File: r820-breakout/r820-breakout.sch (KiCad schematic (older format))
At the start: 18 parts, among them J1 Conn_Coaxial, J2 Conn_01x10, J3 Conn_01x02, J4 Conn_01x02, U1 R820T, Y1 16MHz CL=16pF

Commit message: Heavily reworked.
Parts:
- removed J3: Conn_01x02, Connector_PinHeader_2.54mm:PinHeader_1x02_P2.54mm_Vertical, symbol Connector_Generic:Conn_01x02
- removed Y1: 16MHz CL=16pF, Crystal:Crystal_HC49-4H_Vertical, symbol Device:Crystal_Small
- added C10, C11: C, Capacitors_SMD:C_0402, symbol device:C
- added C12: 330p, Capacitors_SMD:C_0603, symbol device:C
- added C13: 10n, Capacitors_SMD:C_0603, symbol device:C
- added C14: 100n, Capacitors_SMD:C_0603, symbol device:C
- added C15, C16: 100nF, Capacitors_SMD:C_0402, symbol r820-breakout-rescue:C_Small-Device
- added D1: BAV99, TO_SOT_Packages_SMD:SOT-23, symbol Diode:BAV99
- added L3: 8.2n, Inductors_SMD:L_0603, symbol device:L
- added L4: 180n, Inductors_SMD:L_0603, symbol device:L
- added Y1: Crystal_GND24, Crystals:Crystal_SMD_TXC_7M-4pin_3.2x2.5mm, symbol device:Crystal_GND24
- C1, C2, C3, C5: footprint Capacitor_SMD:C_0603_1608Metric -> Capacitors_SMD:C_0402; symbol Device:C_Small -> r820-breakout-rescue:C_Small-Device
- C4, C6, C7, C8, C9: symbol Device:C_Small -> r820-breakout-rescue:C_Small-Device
- J1: footprint Connector_Coaxial:SMA_Molex_73251-2200_Horizontal -> Connectors_Molex:Molex_SMA_Jack_Edge_Mount; symbol Connector:Conn_Coaxial -> r820-breakout-rescue:Conn_Coaxial-Connector
- J2: symbol Connector_Generic:Conn_01x10 -> r820-breakout-rescue:Conn_01x10-Connector_Generic
- J4: symbol Connector_Generic:Conn_01x02 -> r820-breakout-rescue:Conn_01x02-Connector_Generic
- L1, L2: symbol Device:L -> r820-breakout-rescue:L-Device
- R1: symbol Device:R -> r820-breakout-rescue:R-Device
- U1: footprint Sensor_Motion:InvenSense_QFN-24_4x4mm_P0.5mm -> Housings_DFN_QFN:QFN-24-1EP_4x4mm_Pitch0.5mm; symbol RafaelMicro:R820T -> r820-breakout-rescue:R820T-RafaelMicro
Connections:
- net GND: now also J2.2 (Pin_2), J2.5 (Pin_5), J2.7 (Pin_7), U1.25 (EXPAD), C14.1, C15.1, C16.1, D1.1 (A), D1.2 (K), Y1.2, Y1.4; no longer J2.3 (Pin_3), J2.4 (Pin_4), J4.1 (Pin_1)
- net T_CLK_Out: now also J2.6 (Pin_6); no longer J2.7 (Pin_7)
- net T_IF_N: now also C10.2; no longer U1.12 (IF_N)
- net T_IF_P: now also C11.2; no longer U1.13 (IF_P)
- net T_RF_IN: now also C13.1, L4.2; no longer U1.24 (RF-IN)
- net T_SCL: now also J2.3 (Pin_3); no longer J2.6 (Pin_6)
- net T_SDA: now also J2.4 (Pin_4); no longer J2.5 (Pin_5)
- net VDD_3V: now also C15.2, C16.2; no longer J2.2 (Pin_2)
- net at C7.1, U1.8 (XTAL_I): now also Y1.3
- net at C6.1, U1.9 (XTAL_O): now also Y1.1
- new net: C10.1, U1.12 (IF_N)
- new net: C11.1, U1.13 (IF_P)
- new net: L3.2, U1.24 (RF-IN)
- new net: C12.2, L3.1
- new net: C14.2, J4.1 (Pin_1), L4.1
- new net: C12.1, C13.2, D1.3 (A), D1.3 (K)
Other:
- moved on the sheet: J4

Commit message: footprint fix, added OSH logo, removed big via under rt820t
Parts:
- C1, C15, C16, C2, C3, C5: footprint Capacitors_SMD:C_0402 -> Capacitor_SMD:C_0402_1005Metric; symbol r820-breakout-rescue:C_Small-Device -> r820-breakout-rescue:C_Small-Device-r820-breakout-rescue
- C10, C11: footprint Capacitors_SMD:C_0402 -> Capacitor_SMD:C_0402_1005Metric; symbol device:C -> r820-breakout-rescue:C-device
- C12, C13, C14: footprint Capacitors_SMD:C_0603 -> Capacitor_SMD:C_0603_1608Metric; symbol device:C -> r820-breakout-rescue:C-device
- C4, C6, C7, C8, C9: symbol r820-breakout-rescue:C_Small-Device -> r820-breakout-rescue:C_Small-Device-r820-breakout-rescue
- D1: footprint TO_SOT_Packages_SMD:SOT-23 -> Package_TO_SOT_SMD:SOT-23
- J1: symbol r820-breakout-rescue:Conn_Coaxial-Connector -> r820-breakout-rescue:Conn_Coaxial-Connector-r820-breakout-rescue
- J2: symbol r820-breakout-rescue:Conn_01x10-Connector_Generic -> r820-breakout-rescue:Conn_01x10-Connector_Generic-r820-breakout-rescue
- J4: symbol r820-breakout-rescue:Conn_01x02-Connector_Generic -> r820-breakout-rescue:Conn_01x02-Connector_Generic-r820-breakout-rescue
- L1, L2: symbol r820-breakout-rescue:L-Device -> r820-breakout-rescue:L-Device-r820-breakout-rescue
- L3, L4: footprint Inductors_SMD:L_0603 -> Inductor_SMD:L_0603_1608Metric; symbol device:L -> r820-breakout-rescue:L-device
- R1: symbol r820-breakout-rescue:R-Device -> r820-breakout-rescue:R-Device-r820-breakout-rescue
- U1: footprint Housings_DFN_QFN:QFN-24-1EP_4x4mm_Pitch0.5mm -> Package_DFN_QFN:QFN-24-1EP_4x4mm_P0.5mm_EP2.7x2.7mm_ThermalVias; symbol r820-breakout-rescue:R820T-RafaelMicro -> r820-breakout-rescue:R820T-RafaelMicro-r820-breakout-rescue
- Y1: footprint Crystals:Crystal_SMD_TXC_7M-4pin_3.2x2.5mm -> Crystal:Crystal_SMD_TXC_7M-4Pin_3.2x2.5mm; symbol device:Crystal_GND24 -> r820-breakout-rescue:Crystal_GND24-device
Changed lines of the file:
@@
 $EndDescr
 $Comp
-L r820-breakout-rescue:R820T-RafaelMicro U1
+L r820-breakout-rescue:R820T-RafaelMicro-r820-breakout-rescue U1
 U 1 1 5CDEF36B
 P 4400 3650
 F 0 "U1" H 4800 2850 50  0000 C CNN
 F 1 "R820T" H 4800 2750 50  0000 C CNN
-F 2 "Housings_DFN_QFN:QFN-24-1EP_4x4mm_Pitch0.5mm" H 4450 3650 50  0001 C CNN
+F 2 "Package_DFN_QFN:QFN-24-1EP_4x4mm_P0.5mm_EP2.7x2.7mm_ThermalVias" H 4450 3650 50  0001 C CNN
 F 3 "" H 4450 3650 50  0001 C CNN
 	1    4400 3650
@@
 $EndComp
 $Comp
-L r820-breakout-rescue:C_Small-Device C5
+L r820-breakout-rescue:C_Small-Device-r820-breakout-rescue C5
 U 1 1 5CDEF46F
 P 3100 3200
 F 0 "C5" V 3329 3200 50  0000 C CNN
 F 1 "100nF" V 3238 3200 50  0000 C CNN
-F 2 "Capacitors_SMD:C_0402" H 3100 3200 50  0001 C CNN
+F 2 "Capacitor_SMD:C_0402_1005Metric" H 3100 3200 50  0001 C CNN
 F 3 "~" H 3100 3200 50  0001 C CNN
 	1    3100 3200
@@
 $EndComp
 $Comp
-L r820-breakout-rescue:C_Small-Device C4
+L r820-breakout-rescue:C_Small-Device-r820-breakout-rescue C4
 U 1 1 5CDEF4C6
 P 2700 3100
@@
 $EndComp
 $Comp
-L r820-breakout-rescue:C_Small-Device C6
+L r820-breakout-rescue:C_Small-Device-r820-breakout-rescue C6
 U 1 1 5CDEF8DA
 P 2850 4300
@@
 $EndComp
 $Comp
-L r820-breakout-rescue:C_Small-Device C7
+L r820-breakout-rescue:C_Small-Device-r820-breakout-rescue C7
 U 1 1 5CDEF920
 P 3150 4300
@@
 T_IF_AGC
 $Comp
-L r820-breakout-rescue:R-Device R1
+L r820-breakout-rescue:R-Device-r820-breakout-rescue R1
 U 1 1 5CDF60D3
 P 5850 4150
@@
 $EndComp
 $Comp
-L r820-breakout-rescue:C_Small-Device C9
+L r820-breakout-rescue:C_Small-Device-r820-breakout-rescue C9
 U 1 1 5CDF73BF
 P 6250 4500
@@
 $EndComp
 $Comp
-L r820-breakout-rescue:C_Small-Device C8
+L r820-breakout-rescue:C_Small-Device-r820-breakout-rescue C8
 U 1 1 5CDF86FE
 P 5850 4500
@@
 	5500 3950 5000 3950
 $Comp
-L r820-breakout-rescue:L-Device L2
+L r820-breakout-rescue:L-Device-r820-breakout-rescue L2
 U 1 1 5CE049F6
 P 5300 3650
@@
 $EndComp
 $Comp
-L r820-breakout-rescue:L-Device L1
+L r820-breakout-rescue:L-Device-r820-breakout-rescue L1
 U 1 1 5CE06D89
 P 5300 3450
@@
 $EndComp
 $Comp
-L r820-breakout-rescue:C_Small-Device C3
+L r820-breakout-rescue:C_Small-Device-r820-breakout-rescue C3
 U 1 1 5CE0C2BA
 P 4700 2450
-F 0 "C3" H 5400 2500 50  0000 L CNN
-F 1 "100nF" H 5400 2400 50  0000 L CNN
-F 2 "Capacitors_SMD:C_0402" H 4700 2450 50  0001 C CNN
+F 0 "C3" H 4700 3200 50  0000 L CNN
+F 1 "100nF" H 4700 3100 50  0000 L CNN
+F 2 "Capacitor_SMD:C_0402_1005Metric" H 4700 2450 50  0001 C CNN
 F 3 "~" H 4700 2450 50  0001 C CNN
 	1    4700 2450
@@
 $EndComp
 $Comp
-L r820-breakout-rescue:C_Small-Device C2
+L r820-breakout-rescue:C_Small-Device-r820-breakout-rescue C2
 U 1 1 5CE0C345
 P 4500 2450
-F 0 "C2" H 5150 2500 50  0000 L CNN
-F 1 "10nF" H 5150 2400 50  0000 L CNN
-F 2 "Capacitors_SMD:C_0402" H 4500 2450 50  0001 C CNN
+F 0 "C2" H 4500 3200 50  0000 L CNN
+F 1 "10nF" H 4500 3100 50  0000 L CNN
+F 2 "Capacitor_SMD:C_0402_1005Metric" H 4500 2450 50  0001 C CNN
 F 3 "~" H 4500 2450 50  0001 C CNN
 	1    4500 2450
@@
 NoConn ~ 5000 3050
 $Comp
-L r820-breakout-rescue:C_Small-Device C1
+L r820-breakout-rescue:C_Small-Device-r820-breakout-rescue C1
 U 1 1 5CE150EA
 P 4300 2450
-F 0 "C1" H 4850 2500 50  0000 L CNN
-F 1 "100nF" H 4850 2400 50  0000 L CNN
-F 2 "Capacitors_SMD:C_0402" H 4300 2450 50  0001 C CNN
+F 0 "C1" H 4300 3400 50  0000 L CNN
+F 1 "100nF" H 4300 3300 50  0000 L CNN
+F 2 "Capacitor_SMD:C_0402_1005Metric" H 4300 2450 50  0001 C CNN
 F 3 "~" H 4300 2450 50  0001 C CNN
 	1    4300 2450
@@
 	9100 2900 8900 2900
 $Comp
-L r820-breakout-rescue:Conn_Coaxial-Connector J1
+L r820-breakout-rescue:Conn_Coaxial-Connector-r820-breakout-rescue J1
 U 1 1 5CE52A4C
 P 9300 1300
@@
 	9300 1500 9300 1600
 $Comp
-L r820-breakout-rescue:Conn_01x02-Connector_Generic J4
+L r820-breakout-rescue:Conn_01x02-Connector_Generic-r820-breakout-rescue J4
 U 1 1 5CE56D37
 P 7520 2790
@@
 	3600 3950 3600 4900
 $Comp
-L device:Crystal_GND24 Y1
+L r820-breakout-rescue:Crystal_GND24-device Y1
 U 1 1 5CE32966
 P 3000 3960
 F 0 "Y1" H 2810 4006 50  0000 R CNN
 F 1 "Crystal_GND24" H 2810 3915 50  0000 R CNN
-F 2 "Crystals:Crystal_SMD_TXC_7M-4pin_3.2x2.5mm" H 3000 3960 50  0001 C CNN
+F 2 "Crystal:Crystal_SMD_TXC_7M-4Pin_3.2x2.5mm" H 3000 3960 50  0001 C CNN
 F 3 "" H 3000 3960 50  0001 C CNN
 	1    3000 3960
@@
 	8900 2400 9100 2400
 $Comp
-L device:C C10
+L r820-breakout-rescue:C-device C10
 U 1 1 5CE3EC04
 P 5300 4300
 F 0 "C10" H 5415 4346 50  0000 L CNN
 F 1 "C" H 5415 4255 50  0000 L CNN
-F 2 "Capacitors_SMD:C_0402" H 5338 4150 50  0001 C CNN
+F 2 "Capacitor_SMD:C_0402_1005Metric" H 5338 4150 50  0001 C CNN
 F 3 "" H 5300 4300 50  0001 C CNN
 	1    5300 4300
@@
 $EndComp
 $Comp
-L device:C C11
+L r820-breakout-rescue:C-device C11
 U 1 1 5CE3ED03
 P 5400 4540
 F 0 "C11" H 5515 4586 50  0000 L CNN
 F 1 "C" H 5515 4495 50  0000 L CNN
-F 2 "Capacitors_SMD:C_0402" H 5438 4390 50  0001 C CNN
+F 2 "Capacitor_SMD:C_0402_1005Metric" H 5438 4390 50  0001 C CNN
 F 3 "" H 5400 4540 50  0001 C CNN
 	1    5400 4540
@@
 	5400 4390 5400 4050
 $Comp
-L device:L L3
+L r820-breakout-rescue:L-device L3
 U 1 1 5CE3F48A
 P 5900 3200
 F 0 "L3" V 5722 3200 50  0000 C CNN
 F 1 "8.2n" V 5813 3200 50  0000 C CNN
-F 2 "Inductors_SMD:L_0603" H 5900 3200 50  0001 C CNN
+F 2 "Inductor_SMD:L_0603_1608Metric" H 5900 3200 50  0001 C CNN
 F 3 "" H 5900 3200 50  0001 C CNN
 	1    5900 3200
@@
 $EndComp
 $Comp
-L device:L L4
+L r820-breakout-rescue:L-device L4
 U 1 1 5CE3F55B
 P 7070 2950
 F 0 "L4" H 7123 2996 50  0000 L CNN
 F 1 "180n" H 7123 2905 50  0000 L CNN
-F 2 "Inductors_SMD:L_0603" H 7070 2950 50  0001 C CNN
+F 2 "Inductor_SMD:L_0603_1608Metric" H 7070 2950 50  0001 C CNN
 F 3 "" H 7070 2950 50  0001 C CNN
 	1    7070 2950
@@
 $EndComp
 $Comp
-L device:C C12
+L r820-breakout-rescue:C-device C12
 U 1 1 5CE3F65C
 P 6260 3200
 F 0 "C12" V 6008 3200 50  0000 C CNN
 F 1 "330p" V 6099 3200 50  0000 C CNN
-F 2 "Capacitors_SMD:C_0603" H 6298 3050 50  0001 C CNN
+F 2 "Capacitor_SMD:C_0603_1608Metric" H 6298 3050 50  0001 C CNN
 F 3 "" H 6260 3200 50  0001 C CNN
 	1    6260 3200
@@
 $EndComp
 $Comp
-L device:C C13
+L r820-breakout-rescue:C-device C13
 U 1 1 5CE3F77D
 P 6770 3200
 F 0 "C13" V 6518 3200 50  0000 C CNN
 F 1 "10n" V 6609 3200 50  0000 C CNN
-F 2 "Capacitors_SMD:C_0603" H 6808 3050 50  0001 C CNN
+F 2 "Capacitor_SMD:C_0603_1608Metric" H 6808 3050 50  0001 C CNN
 F 3 "" H 6770 3200 50  0001 C CNN
 	1    6770 3200
@@
 F 0 "D1" V 6404 3498 50  0000 L CNN
 F 1 "BAV99" V 6495 3498 50  0000 L CNN
-F 2 "TO_SOT_Packages_SMD:SOT-23" H 6450 3270 50  0001 C CNN
+F 2 "Package_TO_SOT_SMD:SOT-23" H 6450 3270 50  0001 C CNN
 F 3 "www.nxp.com/documents/data_sheet/BAV99_SER.pdf" H 6450 3520 50  0001 C CNN
 	2    6450 3420
@@
 F 0 "D1" V 6626 3497 50  0000 L CNN
 F 1 "BAV99" V 6535 3497 50  0000 L CNN
-F 2 "TO_SOT_Packages_SMD:SOT-23" H 6580 3270 50  0001 C CNN
+F 2 "Package_TO_SOT_SMD:SOT-23" H 6580 3270 50  0001 C CNN
 F 3 "www.nxp.com/documents/data_sheet/BAV99_SER.pdf" H 6580 3520 50  0001 C CNN
 	1    6580 3420
@@
 	7320 2890 7320 2920
 $Comp
-L device:C C14
+L r820-breakout-rescue:C-device C14
 U 1 1 5CE5F008
 P 7070 2630
 F 0 "C14" H 7185 2676 50  0000 L CNN
 F 1 "100n" H 7185 2585 50  0000 L CNN
-F 2 "Capacitors_SMD:C_0603" H 7108 2480 50  0001 C CNN
+F 2 "Capacitor_SMD:C_0603_1608Metric" H 7108 2480 50  0001 C CNN
 F 3 "" H 7070 2630 50  0001 C CNN
 	1    7070 2630
@@
 	4600 4550 4600 4650
 $Comp
-L r820-breakout-rescue:C_Small-Device C16
+L r820-breakout-rescue:C_Small-Device-r820-breakout-rescue C16
 U 1 1 5CE454F0
 P 4100 2440
-F 0 "C16" H 4650 2490 50  0000 L CNN
-F 1 "100nF" H 4650 2390 50  0000 L CNN
-F 2 "Capacitors_SMD:C_0402" H 4100 2440 50  0001 C CNN
+F 0 "C16" H 4100 3180 50  0000 L CNN
+F 1 "100nF" H 4100 3080 50  0000 L CNN
+F 2 "Capacitor_SMD:C_0402_1005Metric" H 4100 2440 50  0001 C CNN
 F 3 "~" H 4100 2440 50  0001 C CNN
 	1    4100 2440
@@
 $EndComp
 $Comp
-L r820-breakout-rescue:C_Small-Device C15
+L r820-breakout-rescue:C_Small-Device-r820-breakout-rescue C15
 U 1 1 5CE455A4
 P 3930 2440
-F 0 "C15" H 4480 2490 50  0000 L CNN
-F 1 "100nF" H 4480 2390 50  0000 L CNN
-F 2 "Capacitors_SMD:C_0402" H 3930 2440 50  0001 C CNN
+F 0 "C15" H 3900 3380 50  0000 L CNN
+F 1 "100nF" H 3900 3280 50  0000 L CNN
+F 2 "Capacitor_SMD:C_0402_1005Metric" H 3930 2440 50  0001 C CNN
 F 3 "~" H 3930 2440 50  0001 C CNN
 	1    3930 2440
@@
 	4100 2340 4100 2200
 $Comp
-L r820-breakout-rescue:Conn_01x10-Connector_Generic J2
+L r820-breakout-rescue:Conn_01x10-Connector_Generic-r820-breakout-rescue J2
 U 1 1 5CE416C7
 P 9300 2400
@@
 $EndComp
 $Comp
-L power:GND #PWR?
+L power:GND #PWR0104
 U 1 1 5CE574E3
 P 8890 2600
-F 0 "#PWR?" H 8890 2350 50  0001 C CNN
+F 0 "#PWR0104" H 8890 2350 50  0001 C CNN
 F 1 "GND" V 8895 2472 50  0000 R CNN
 F 2 "" H 8890 2600 50  0001 C CNN

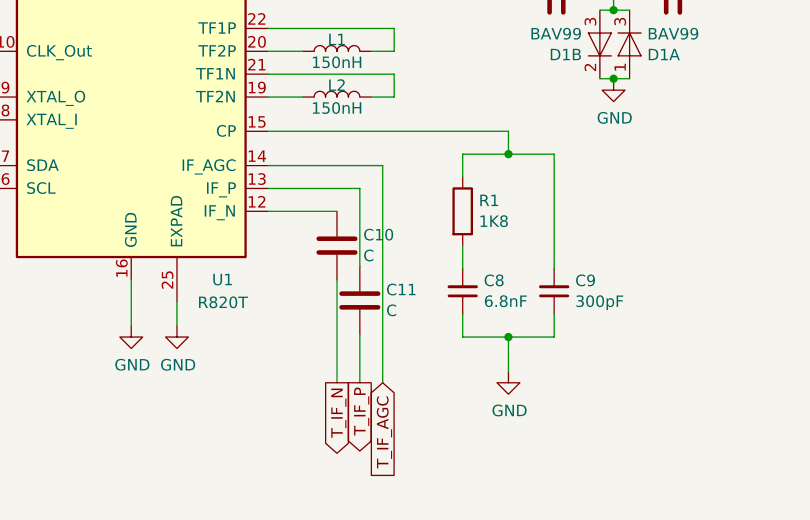
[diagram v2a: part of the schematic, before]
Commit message: Fix F.Cu fill zone clearance
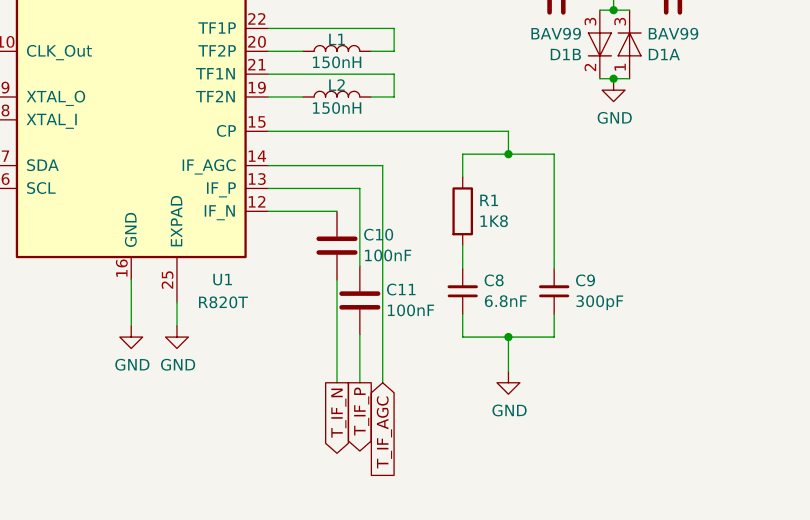
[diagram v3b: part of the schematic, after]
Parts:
- C10, C11: value C -> 100nF
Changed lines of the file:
@@
 P 5300 4300
 F 0 "C10" H 5415 4346 50  0000 L CNN
-F 1 "C" H 5415 4255 50  0000 L CNN
+F 1 "100nF" H 5415 4255 50  0000 L CNN
 F 2 "Capacitor_SMD:C_0402_1005Metric" H 5338 4150 50  0001 C CNN
 F 3 "" H 5300 4300 50  0001 C CNN
@@
 P 5400 4540
 F 0 "C11" H 5515 4586 50  0000 L CNN
-F 1 "C" H 5515 4495 50  0000 L CNN
+F 1 "100nF" H 5515 4495 50  0000 L CNN
 F 2 "Capacitor_SMD:C_0402_1005Metric" H 5438 4390 50  0001 C CNN
 F 3 "" H 5400 4540 50  0001 C CNN

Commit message: fix some value
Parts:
- C12: value 330p -> 330pF
- C13: value 10n -> 10nF
- L3: value 8.2n -> 8.2nH
- L4: value 180n -> 180nH
- Y1: value Crystal_GND24 -> 16MHz
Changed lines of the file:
@@
 P 3000 3960
 F 0 "Y1" H 2810 4006 50  0000 R CNN
-F 1 "Crystal_GND24" H 2810 3915 50  0000 R CNN
+F 1 "16MHz" H 2810 3915 50  0000 R CNN
 F 2 "Crystal:Crystal_SMD_TXC_7M-4Pin_3.2x2.5mm" H 3000 3960 50  0001 C CNN
 F 3 "" H 3000 3960 50  0001 C CNN
@@
 P 5900 3200
 F 0 "L3" V 5722 3200 50  0000 C CNN
-F 1 "8.2n" V 5813 3200 50  0000 C CNN
+F 1 "8.2nH" V 5813 3200 50  0000 C CNN
 F 2 "Inductor_SMD:L_0603_1608Metric" H 5900 3200 50  0001 C CNN
 F 3 "" H 5900 3200 50  0001 C CNN
@@
 P 7070 2950
 F 0 "L4" H 7123 2996 50  0000 L CNN
-F 1 "180n" H 7123 2905 50  0000 L CNN
+F 1 "180nH" H 7123 2905 50  0000 L CNN
 F 2 "Inductor_SMD:L_0603_1608Metric" H 7070 2950 50  0001 C CNN
 F 3 "" H 7070 2950 50  0001 C CNN
@@
 P 6260 3200
 F 0 "C12" V 6008 3200 50  0000 C CNN
-F 1 "330p" V 6099 3200 50  0000 C CNN
+F 1 "330pF" V 6099 3200 50  0000 C CNN
 F 2 "Capacitor_SMD:C_0603_1608Metric" H 6298 3050 50  0001 C CNN
 F 3 "" H 6260 3200 50  0001 C CNN
@@
 P 6770 3200
 F 0 "C13" V 6518 3200 50  0000 C CNN
-F 1 "10n" V 6609 3200 50  0000 C CNN
+F 1 "10nF" V 6609 3200 50  0000 C CNN
 F 2 "Capacitor_SMD:C_0603_1608Metric" H 6808 3050 50  0001 C CNN
 F 3 "" H 6770 3200 50  0001 C CNN
